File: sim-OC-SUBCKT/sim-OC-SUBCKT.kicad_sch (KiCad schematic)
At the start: 21 parts, among them U4 74AHC1G02, U5 MCP6561-OT, U6 MCP6561-OT

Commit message: working on sim files, made updates to sim models, trying to fix issue on linux
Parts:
- removed D4: GREEN, symbol Device:LED
- removed D5: RED, symbol Device:LED
- removed D6: WHITE, symbol Device:LED
- removed R21: 1.45k, symbol Device:R_US
- removed R22: 1.6k, symbol Device:R_US
- removed R23: 370, symbol Device:R_US
- R10: value 10k -> ${SIM.PARAMS}
- R19: value 9.9k -> 96k
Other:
- moved on the sheet: V1

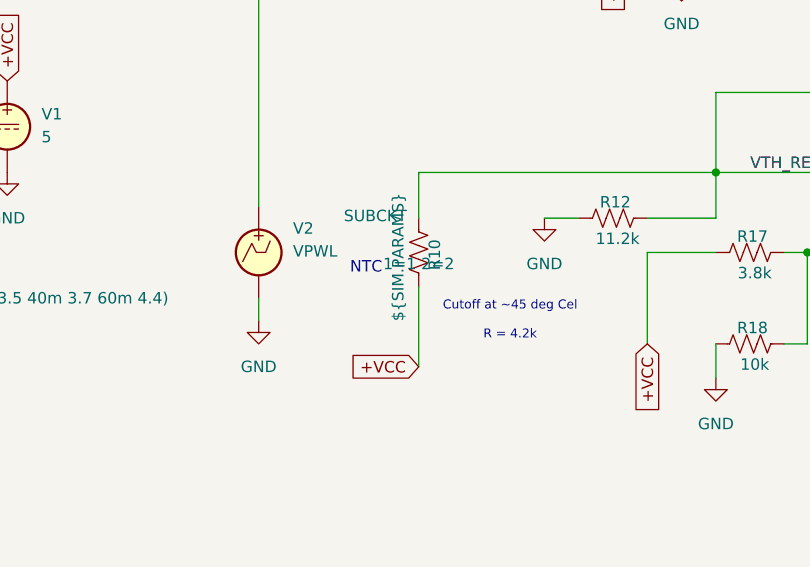
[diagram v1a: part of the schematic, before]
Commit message: updated simulation parameters, and adjusted file locations
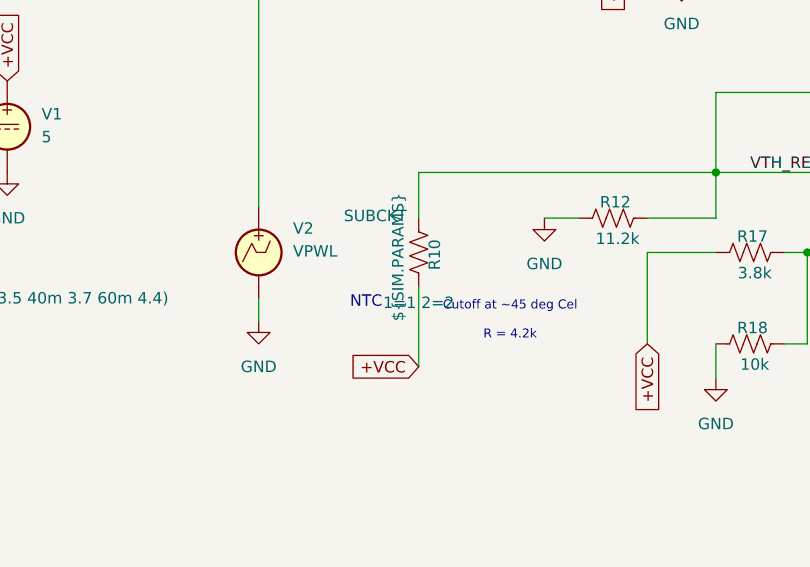
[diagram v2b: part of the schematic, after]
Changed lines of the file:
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@@
 	(text "NTC\n"
 		(exclude_from_sim no)
-		(at 83.058 118.618 0)
+		(at 83.058 122.428 0)
 		(effects
 			(font
@@
 		)
 		(property "Sim.Pins" "1=1 2=2"
-			(at 88.9 118.11 0)
+			(at 88.9 122.428 0)
 			(show_name no)
 			(do_not_autoplace no)
@@
 			)
 		)
-		(property "Sim.Name" "NTC_2PIN"
+		(property "Sim.Name" "ntc_2pin"
 			(at 88.9 116.84 0)
 			(hide yes)
